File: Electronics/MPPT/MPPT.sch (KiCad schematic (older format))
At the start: 105 parts, among them J1 Solar Array, J2 Battery, J3 Car Power, J4 CAN_In, J5 CAN_Out, Q1 200N25N, Q2 200N25N, SW1 RESET, SW2 CAN Address, U1 PQMC3-D12-S9-S, U2 Nucleo_L432KC, U3 UCC37321, U4 INA213, U5 ADM3055E, U6 INA213, U7 CDSOT23-T24CAN

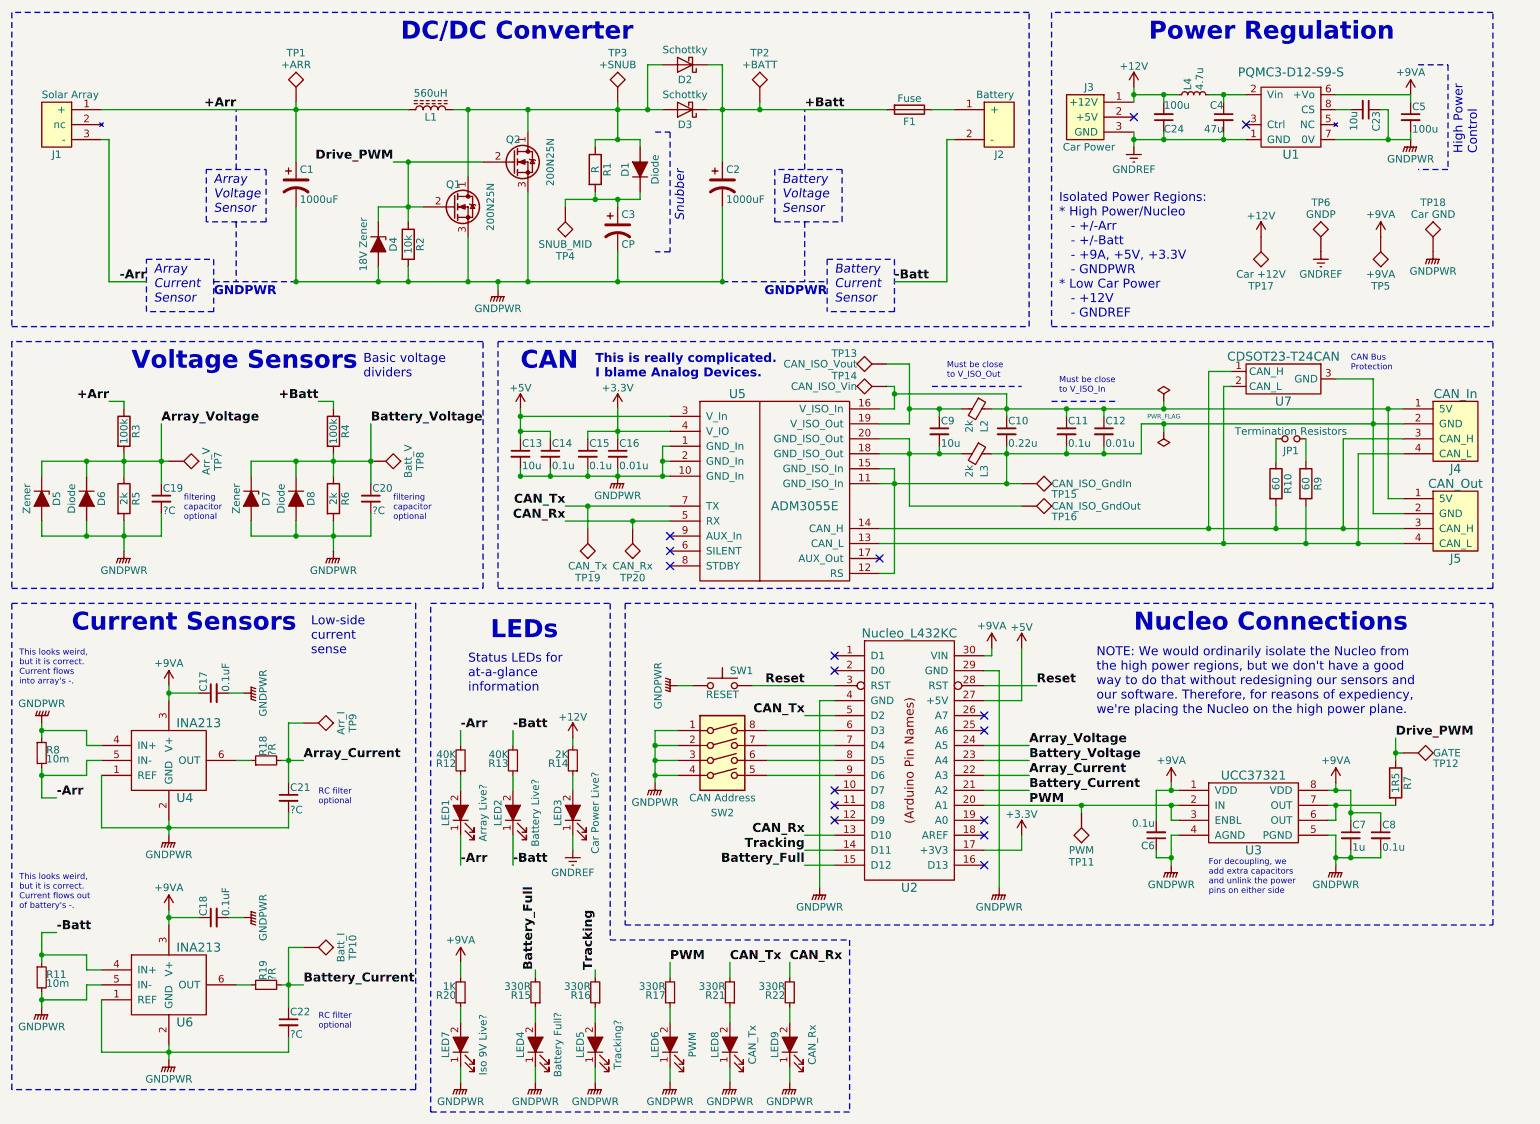
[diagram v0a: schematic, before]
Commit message: MPPT: Add diodes to FET driver input signal.
Also moved FET gate test point to DC/DC convert block in schematic.
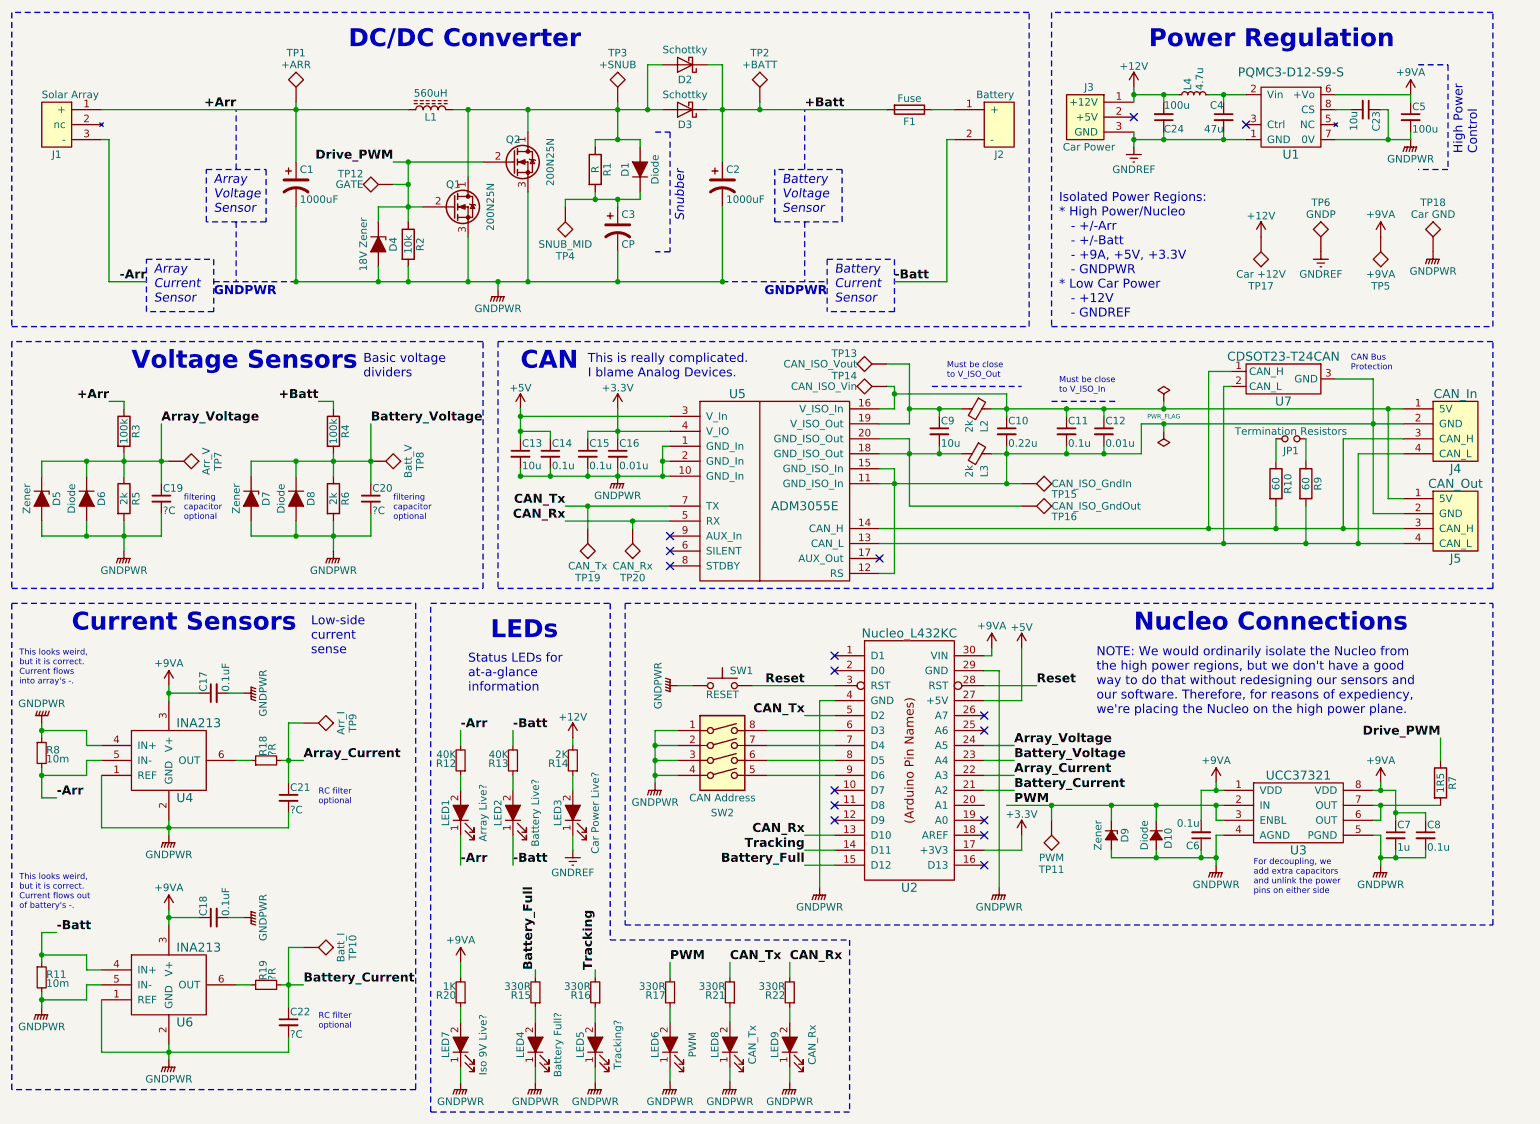
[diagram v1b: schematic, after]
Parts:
- added D10: Diode, Diodes_SMD:D_SOD-123, symbol D_Small_ALT
- added D9: Zener, Diodes_SMD:D_SOD-123F, symbol D_Zener_Small_ALT
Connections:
- net GNDPWR: now also D10.2 (A), D9.2 (A)
- net PWM: now also D10.1 (K), D9.1 (K); no longer U2.20 (A1)
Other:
- moved on the sheet: C6, C7, C8, R7, TP11, TP12, U3

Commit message: MPPT: Add test points to CAN_H and CAN_L lines.
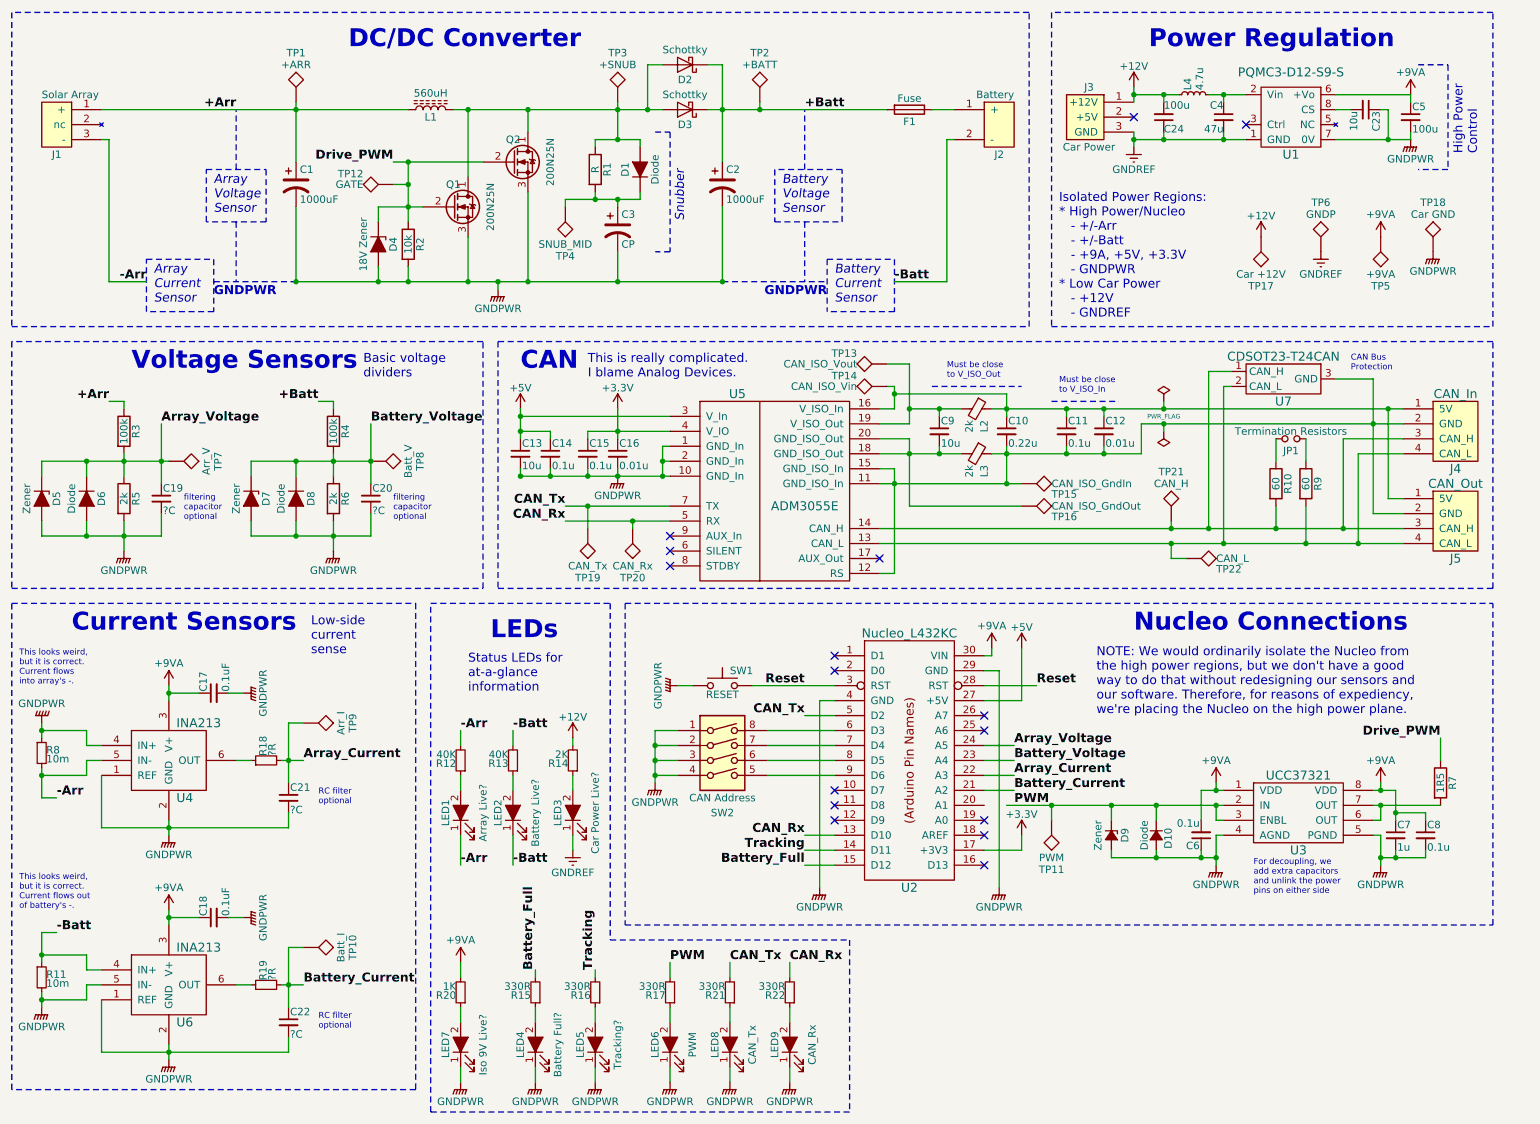
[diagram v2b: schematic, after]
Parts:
- added TP21: CAN_H, Measurement_Points:Test_Point_Keystone_5005-5009_Compact, symbol TEST
- added TP22: CAN_L, Measurement_Points:Test_Point_Keystone_5005-5009_Compact, symbol TEST
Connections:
- net at J4.3 (CAN_H), J5.3 (CAN_H), R10.2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: now also TP21.1
- net at J4.4 (CAN_L), J5.4 (CAN_L), R9.2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: now also TP22.1

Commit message: MPPT: Fix broken PWM output line from Nucleo
I accidentally broke it while moving around the FET driver in a previous commit.
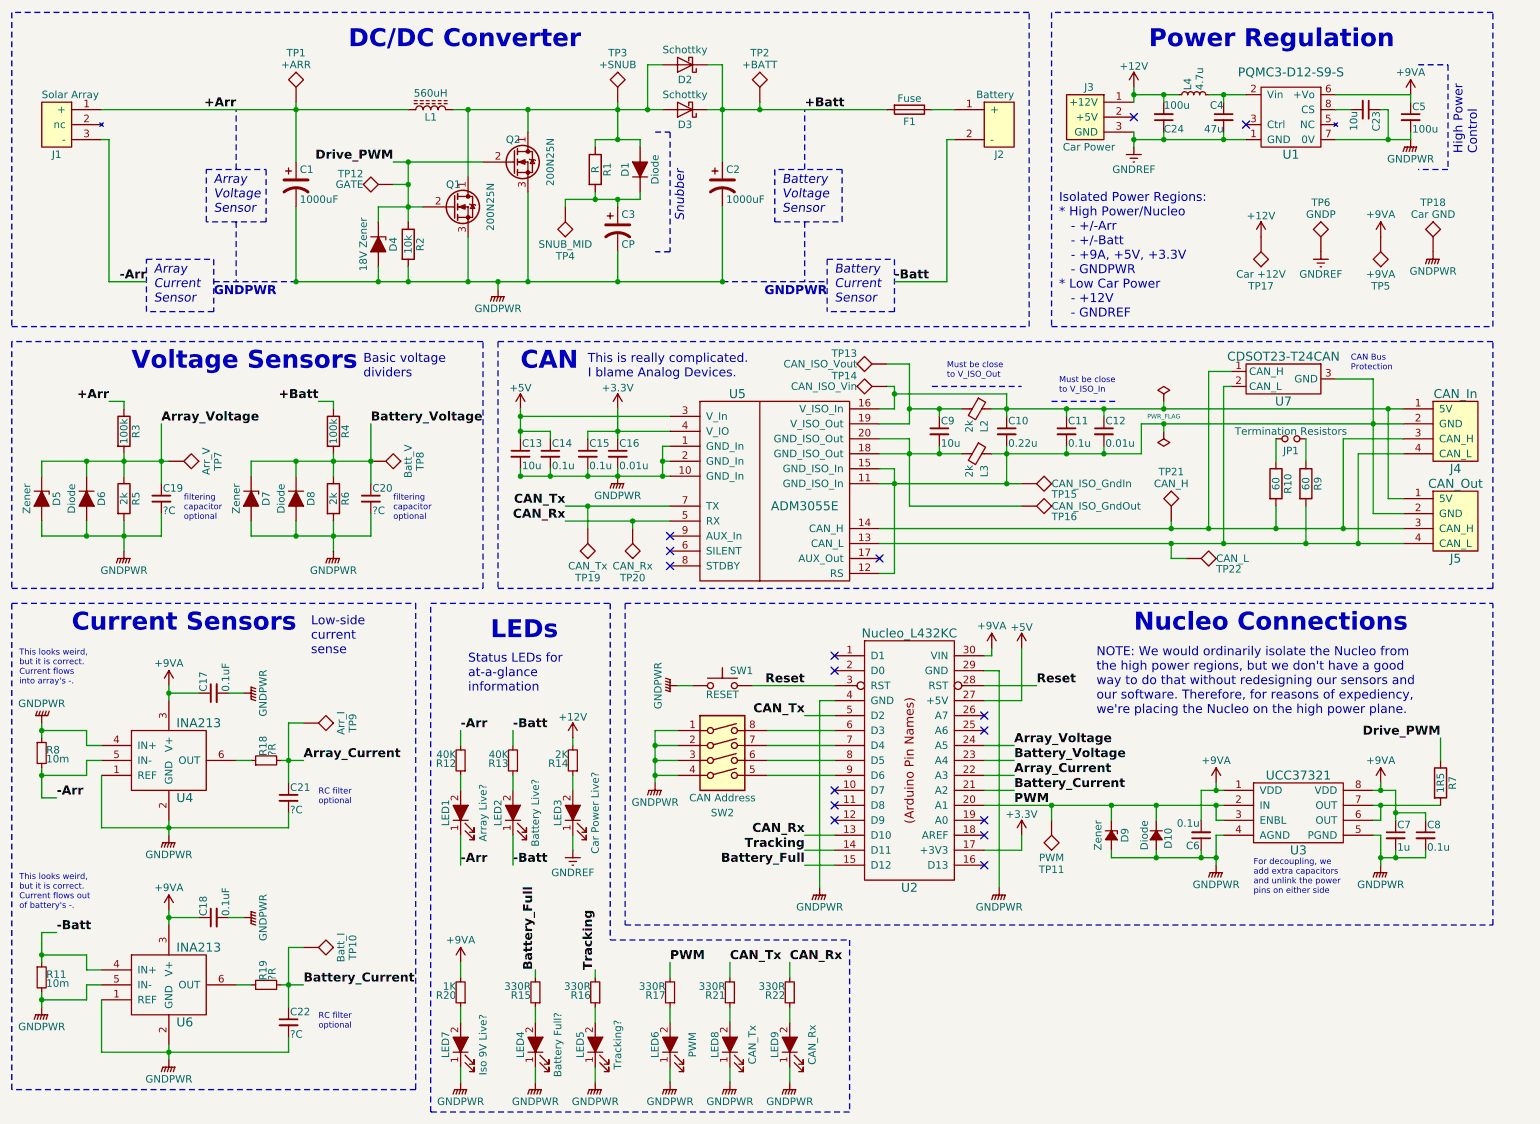
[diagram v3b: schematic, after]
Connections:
- net PWM: now also U2.20 (A1)

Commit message: MPPT: Reduce size of CAN termination resistors from 1206 to 0805.
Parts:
- R10, R9: footprint Resistors_SMD:R_1206_HandSoldering -> Resistors_SMD:R_0805_HandSoldering
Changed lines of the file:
@@
 F 0 "R9" V 9280 3700 50  0000 C CNN
 F 1 "60" V 9200 3700 50  0000 C CNN
-F 2 "Resistors_SMD:R_1206_HandSoldering" V 9130 3700 50  0001 C CNN
+F 2 "Resistors_SMD:R_0805_HandSoldering" V 9130 3700 50  0001 C CNN
 F 3 "" H 9200 3700 50  0001 C CNN
 	1    9200 3700
@@
 F 0 "R10" V 9080 3700 50  0000 C CNN
 F 1 "60" V 9000 3700 50  0000 C CNN
-F 2 "Resistors_SMD:R_1206_HandSoldering" V 8930 3700 50  0001 C CNN
+F 2 "Resistors_SMD:R_0805_HandSoldering" V 8930 3700 50  0001 C CNN
 F 3 "" H 9000 3700 50  0001 C CNN
 	1    9000 3700
